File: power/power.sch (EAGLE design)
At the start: 8 parts, among them IC1 LD117AS33TR, J1 ESP-STACK-HEADER

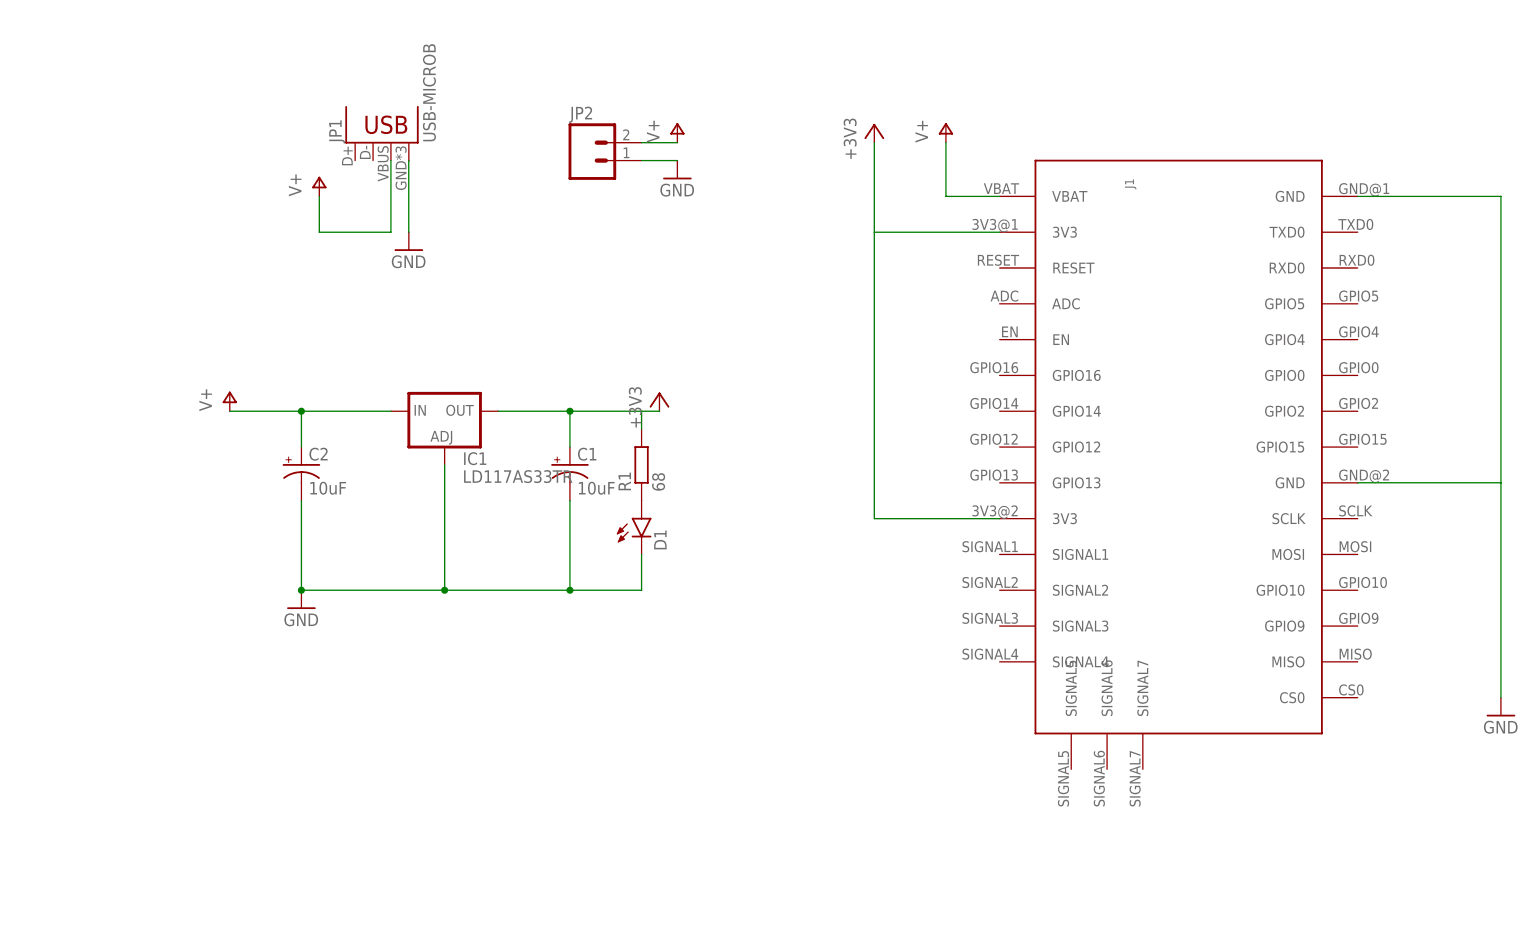
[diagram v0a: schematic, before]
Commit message: Power/FTDI board
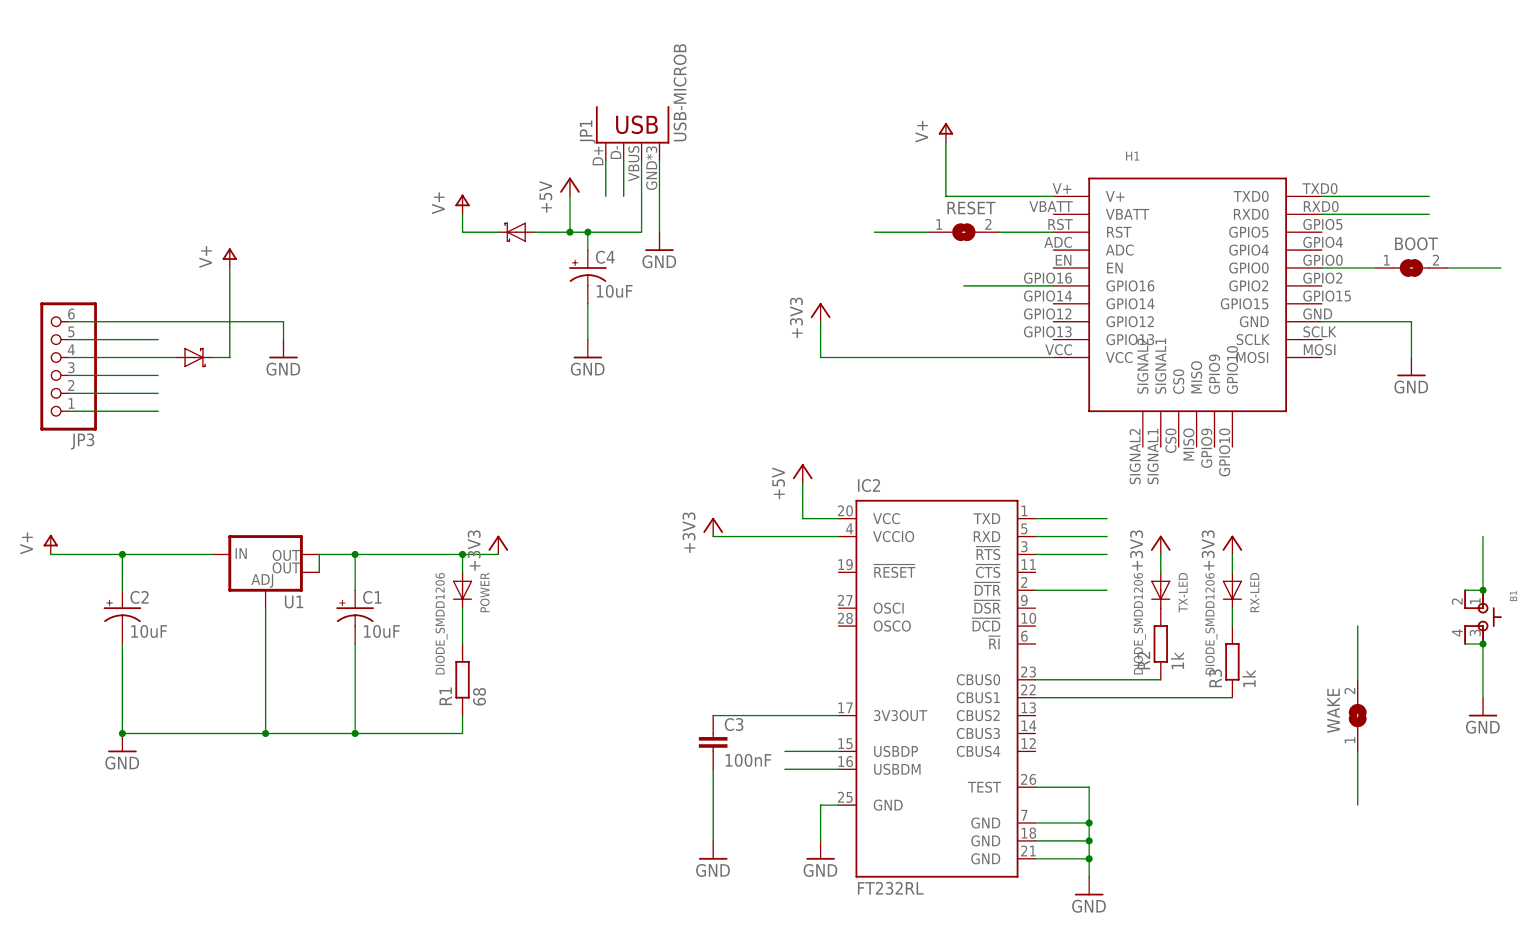
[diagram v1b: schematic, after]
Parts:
- removed IC1: LD117AS33TR, v-reg:LD117AS33TR
- removed J1: ESP-STACK-HEADER, ESPstack:ESP-STACK-HEADER
- removed JP2: (no value), SparkFun-Connectors:M02LOCK_LONGPADS
- added B1: (no value), ESPstack:SKSCLDE010
- added BOOT, RESET, WAKE: (no value), jumper:SJ
- added C3: 100nF, eagle-ltspice:C
- added C4: 10uF, SparkFun-Capacitors:10UF-16V-10%(TANT)
- added D2: MBR120, ESPstack:SCHOTTKY_DIODE_SMDSOD123
- added H1: ESP-BOARD, ESPstack:ESP-BOARD
- added IC2: FT232RL, ftdichip:FT232RL
- added JP3: (no value), pinhead:PINHD-1X6/90
- added POWER, RX-LED, TX-LED: DIODE_SMDD1206, diodes_gen:DIODE_SMDD1206
- added R2, R3: 1k, dp_devices:RESISTOR-1206
- added U1: (no value), SparkFun-PowerIC:V_REG_LM1117SOT223
- D1: value (none) -> MBR120; device SparkFun-LED:LED-FKIT-1206 -> ESPstack:SCHOTTKY_DIODE_SMDSOD123
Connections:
- new net +5V: C4.+, D1.A, IC2.VCC, JP1.VBUS
- new net D+: IC2.USBDP, JP1.D+
- new net D-: IC2.USBDM, JP1.D-
- new net DTR: B1.1, B1.2, BOOT.2, IC2.!DTR, JP3.5
- new net GPIO0: BOOT.1, H1.GPIO0
- new net GPIO16: H1.GPIO16, WAKE.1
- new net N$16: C3.1, IC2.3V3OUT
- new net N$2: IC2.CBUS1, R3.1
- new net N$3: R2.2, TX-LED.K
- new net N$4: IC2.CBUS0, R2.1
- new net N$8: D2.A, JP3.4
- new net N$9: R3.2, RX-LED.K
- new net RST: H1.RST, RESET.2, WAKE.2
- new net RTS: IC2.!RTS, JP3.1, RESET.1
- new net RXD: H1.TXD0, IC2.RXD, JP3.2
- new net TXD: H1.RXD0, IC2.TXD, JP3.3
- net +3V3: now also H1.VCC, IC2.VCCIO, POWER.A, RX-LED.A, TX-LED.A, U1.OUT, U1.OUT@1; no longer IC1.OUT, J1.3V3@1, J1.3V3@2, R1.2
- net GND: now also B1.3, B1.4, C3.2, C4.-, H1.GND, IC2.GND@1, IC2.GND@2, IC2.GND@A, IC2.TEST, JP3.6, R1.1, U1.ADJ; no longer D1.C, IC1.ADJ, J1.GND@1, J1.GND@2, JP2.1
- net N$1: now also POWER.K, R1.2; no longer D1.A, R1.1
- net V+: now also D1.C, D2.C, H1.V+, U1.IN; no longer IC1.IN, J1.VBAT, JP1.VBUS, JP2.2
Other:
- moved on the sheet: C1, C2, JP1, R1

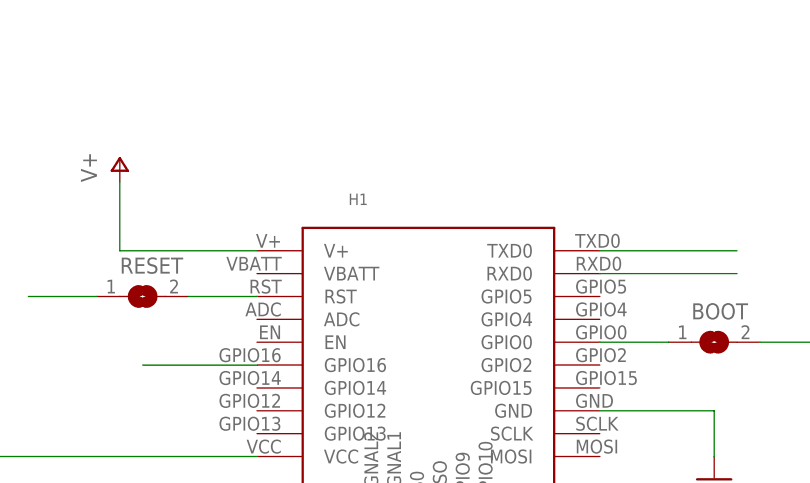
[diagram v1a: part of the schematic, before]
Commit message: Power board (USB, external power, FT232RL section
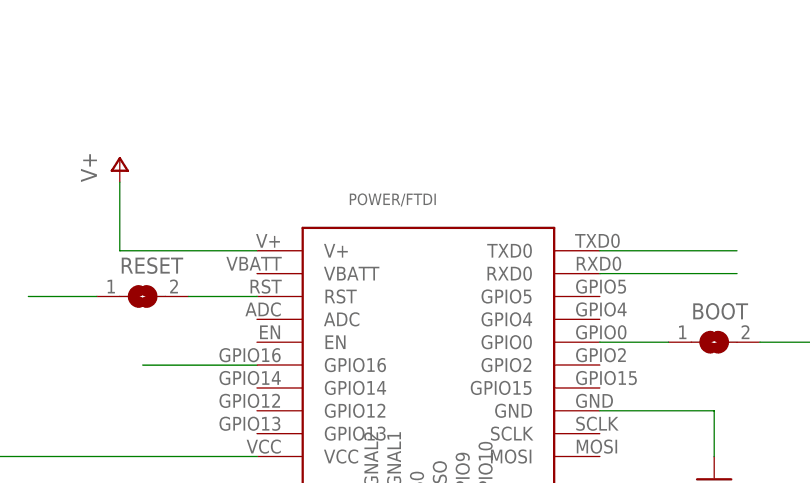
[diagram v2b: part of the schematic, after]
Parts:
- JP3: device pinhead:PINHD-1X6/90 -> ESPstack:PINHD-1X6
- renumbered H1 to POWER/FTDI
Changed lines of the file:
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@@
 <part name="GND3" library="supply1" deviceset="GND" device=""/>
 <part name="R1" library="dp_devices" deviceset="RESISTOR" device="-1206" value="68"/>
-<part name="H1" library="ESPstack" deviceset="ESP-BOARD" device=""/>
+<part name="POWER/FTDI" library="ESPstack" deviceset="ESP-BOARD" device=""/>
 <part name="GND5" library="supply1" deviceset="GND" device=""/>
 <part name="IC2" library="ftdichip" deviceset="FT232R" device="L"/>
@@
 <part name="BOOT" library="jumper" deviceset="SJ" device=""/>
 <part name="RESET" library="jumper" deviceset="SJ" device=""/>
-<part name="JP3" library="pinhead" deviceset="PINHD-1X6" device="/90"/>
+<part name="JP3" library="ESPstack" deviceset="PINHD-1X6" device=""/>
 <part name="C4" library="SparkFun-Capacitors" deviceset="10UF-16V-10%(TANT)" device="" value="10uF"/>
 <part name="GND4" library="supply1" deviceset="GND" device=""/>
@@
 <instance part="GND3" gate="1" x="160.02" y="68.58"/>
 <instance part="R1" gate="G$1" x="25.4" y="25.4" rot="R90"/>
-<instance part="H1" gate="G$1" x="127" y="81.28"/>
+<instance part="POWER/FTDI" gate="G$1" x="127" y="81.28"/>
 <instance part="GND5" gate="1" x="114.3" y="-5.08"/>
 <instance part="IC2" gate="1" x="91.44" y="25.4"/>
@@
 <pinref part="P+2" gate="1" pin="V+"/>
 <wire x1="93.98" y1="93.98" x2="93.98" y2="101.6" width="0.1524" layer="91"/>
-<pinref part="H1" gate="G$1" pin="V+"/>
+<pinref part="POWER/FTDI" gate="G$1" pin="V+"/>
 <wire x1="93.98" y1="93.98" x2="109.22" y2="93.98" width="0.1524" layer="91"/>
 </segment>
@@
 <wire x1="109.22" y1="71.12" x2="76.2" y2="71.12" width="0.1524" layer="91"/>
 <wire x1="76.2" y1="71.12" x2="76.2" y2="76.2" width="0.1524" layer="91"/>
-<pinref part="H1" gate="G$1" pin="VCC"/>
+<pinref part="POWER/FTDI" gate="G$1" pin="VCC"/>
 </segment>
 <segment>
@@
 <wire x1="147.32" y1="76.2" x2="160.02" y2="76.2" width="0.1524" layer="91"/>
 <wire x1="160.02" y1="76.2" x2="160.02" y2="71.12" width="0.1524" layer="91"/>
-<pinref part="H1" gate="G$1" pin="GND"/>
+<pinref part="POWER/FTDI" gate="G$1" pin="GND"/>
 </segment>
 <segment>
@@
 <net name="GPIO0" class="0">
 <segment>
-<pinref part="H1" gate="G$1" pin="GPIO0"/>
+<pinref part="POWER/FTDI" gate="G$1" pin="GPIO0"/>
 <wire x1="147.32" y1="83.82" x2="154.94" y2="83.82" width="0.1524" layer="91"/>
 <pinref part="BOOT" gate="1" pin="1"/>
@@
 </segment>
 <segment>
-<pinref part="H1" gate="G$1" pin="RST"/>
+<pinref part="POWER/FTDI" gate="G$1" pin="RST"/>
 <wire x1="109.22" y1="88.9" x2="101.6" y2="88.9" width="0.1524" layer="91"/>
 <pinref part="RESET" gate="1" pin="2"/>
@@
 </segment>
 <segment>
-<pinref part="H1" gate="G$1" pin="RXD0"/>
+<pinref part="POWER/FTDI" gate="G$1" pin="RXD0"/>
 <wire x1="147.32" y1="91.44" x2="162.56" y2="91.44" width="0.1524" layer="91"/>
 </segment>
@@
 </segment>
 <segment>
-<pinref part="H1" gate="G$1" pin="TXD0"/>
+<pinref part="POWER/FTDI" gate="G$1" pin="TXD0"/>
 <wire x1="147.32" y1="93.98" x2="162.56" y2="93.98" width="0.1524" layer="91"/>
 </segment>
@@
 </segment>
 <segment>
-<pinref part="H1" gate="G$1" pin="GPIO16"/>
+<pinref part="POWER/FTDI" gate="G$1" pin="GPIO16"/>
 <wire x1="109.22" y1="81.28" x2="96.52" y2="81.28" width="0.1524" layer="91"/>
 </segment>

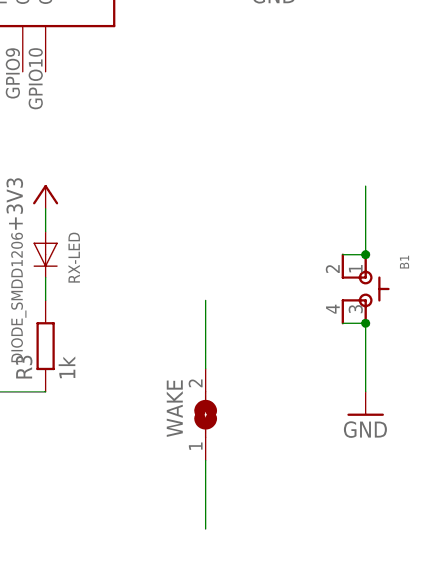
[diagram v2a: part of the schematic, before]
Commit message: Small improvements to usb board
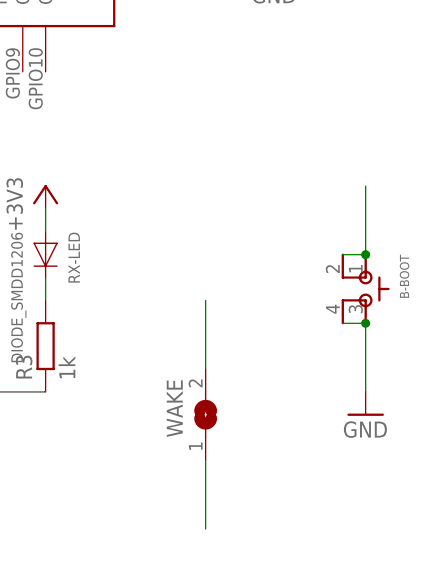
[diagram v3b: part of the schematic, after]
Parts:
- renumbered B1 to B-BOOT
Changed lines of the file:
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@@
 <part name="U1" library="SparkFun-PowerIC" deviceset="V_REG_LM1117" device="SOT223"/>
 <part name="WAKE" library="jumper" deviceset="SJ" device=""/>
-<part name="B1" library="ESPstack" deviceset="SKSCLDE010" device=""/>
+<part name="B-BOOT" library="ESPstack" deviceset="SKSCLDE010" device=""/>
 <part name="GND10" library="supply1" deviceset="GND" device=""/>
 </parts>
@@
 <instance part="U1" gate="G$1" x="-2.54" y="43.18"/>
 <instance part="WAKE" gate="1" x="152.4" y="20.32" rot="R90"/>
-<instance part="B1" gate="G$1" x="170.18" y="33.02" rot="R270"/>
+<instance part="B-BOOT" gate="G$1" x="170.18" y="33.02" rot="R270"/>
 <instance part="GND10" gate="1" x="170.18" y="20.32"/>
 </instances>
@@
 </segment>
 <segment>
-<pinref part="B1" gate="G$1" pin="3"/>
-<pinref part="B1" gate="G$1" pin="4"/>
+<pinref part="B-BOOT" gate="G$1" pin="3"/>
+<pinref part="B-BOOT" gate="G$1" pin="4"/>
 <wire x1="167.64" y1="30.48" x2="170.18" y2="30.48" width="0.1524" layer="91"/>
 <wire x1="170.18" y1="30.48" x2="170.18" y2="22.86" width="0.1524" layer="91"/>
@@
 </segment>
 <segment>
-<pinref part="B1" gate="G$1" pin="2"/>
-<pinref part="B1" gate="G$1" pin="1"/>
+<pinref part="B-BOOT" gate="G$1" pin="2"/>
+<pinref part="B-BOOT" gate="G$1" pin="1"/>
 <wire x1="167.64" y1="38.1" x2="170.18" y2="38.1" width="0.1524" layer="91"/>
 <wire x1="170.18" y1="38.1" x2="170.18" y2="45.72" width="0.1524" layer="91"/>
